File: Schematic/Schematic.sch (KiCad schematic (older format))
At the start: 13 parts, among them P1 Digital, P2 Analog, P3 CONN_01X01, P4 CONN_01X01, P5 CONN_01X01, P6 CONN_01X01

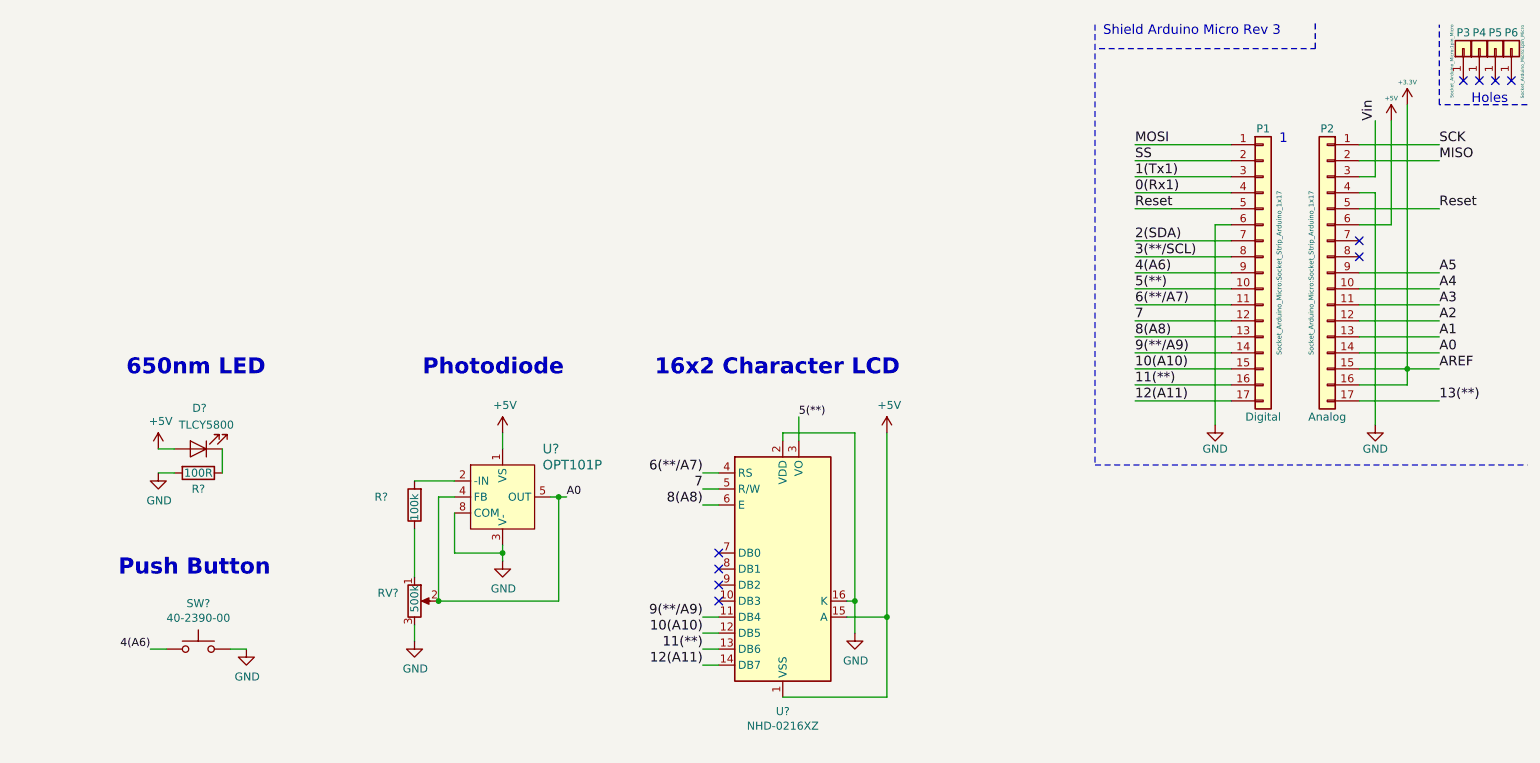
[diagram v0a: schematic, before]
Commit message: Add initial Arduino code
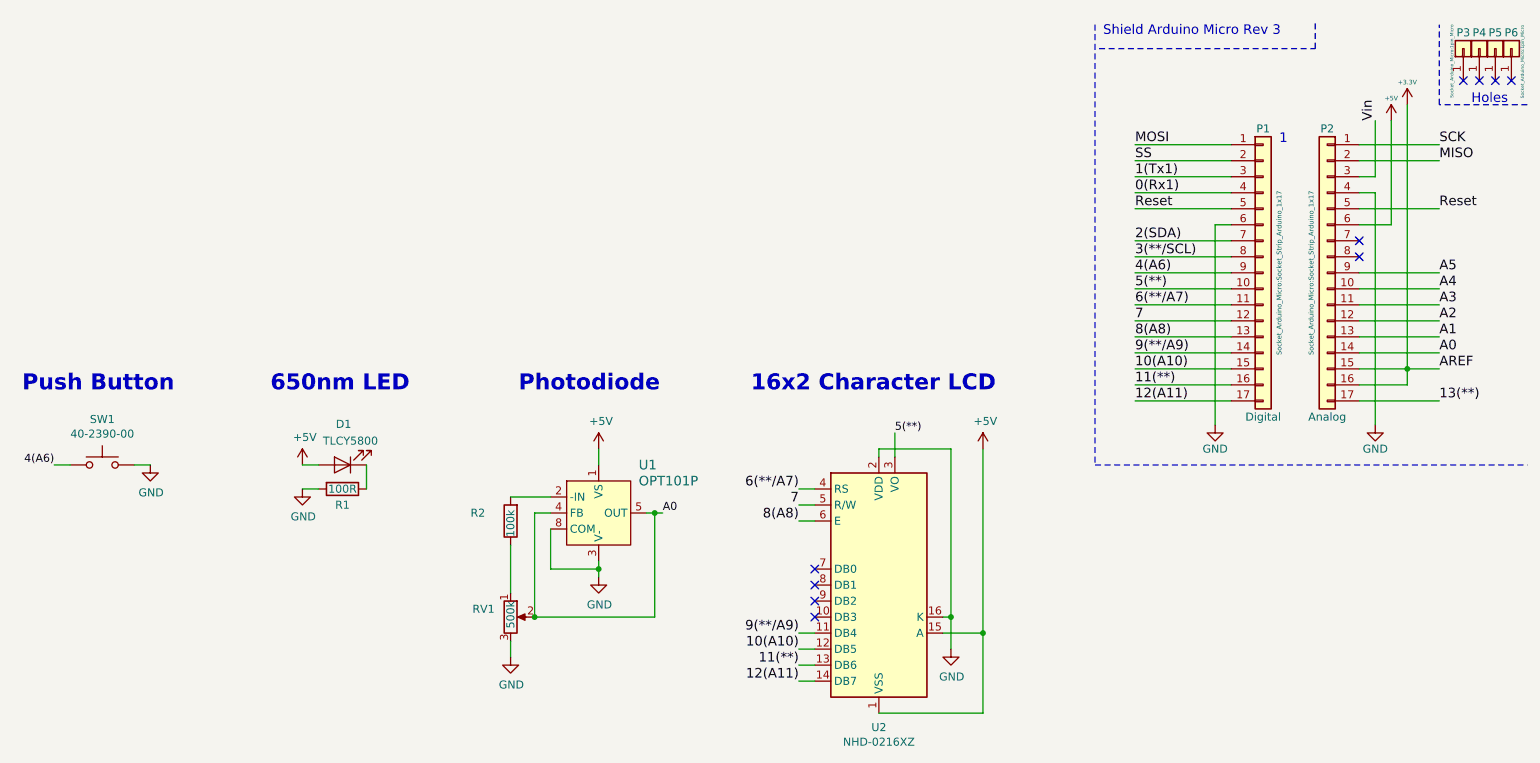
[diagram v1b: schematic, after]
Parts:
- gave numbers to parts that had none: 7
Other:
- moved on the sheet: D1, R1, R2, RV1, SW1, U1, U2
